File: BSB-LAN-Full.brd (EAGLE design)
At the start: 86.5 x 33 mm, 121 parts, among them IC1 LAN8710A-EZC, IC2 TPS2375D, IC3 TX4138, IC4 SY8089AAAC, IC6 CH340X, Q1 BC847, Q2 BC857, Q3 BC847, Q4 WPM2015-3/TR, Q5 BC847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

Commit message: Rename Connector Footprint
Remove special characters
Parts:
- BSB: device BSB-LAN:MKDSN1,5/2-5,08 -> BSB-LAN:MKDSN1_5-2-5_08
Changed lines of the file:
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@@
 <attribute name="NAME" x="27.2" y="32.4" size="0.8" layer="26" font="vector" ratio="15" rot="MR0" align="center"/>
 </element>
-<element name="BSB" library="BSB-LAN" package="MKDSN1,5/2-5,08" value="MKDSN1,5/2-5,08" x="4.96" y="26.66" smashed="yes" rot="R270">
+<element name="BSB" library="BSB-LAN" package="MKDSN1_5-2-5_08" value="MKDSN1,5/2-5,08" x="4.96" y="26.66" smashed="yes" rot="R270">
 <attribute name="NAME" x="11.15" y="31.47" size="1.2" layer="25" font="vector" ratio="15" align="center"/>
 <attribute name="OC_NEWARK" value="30M2397" x="4.96" y="26.66" size="1.778" layer="27" rot="R270" display="off"/>

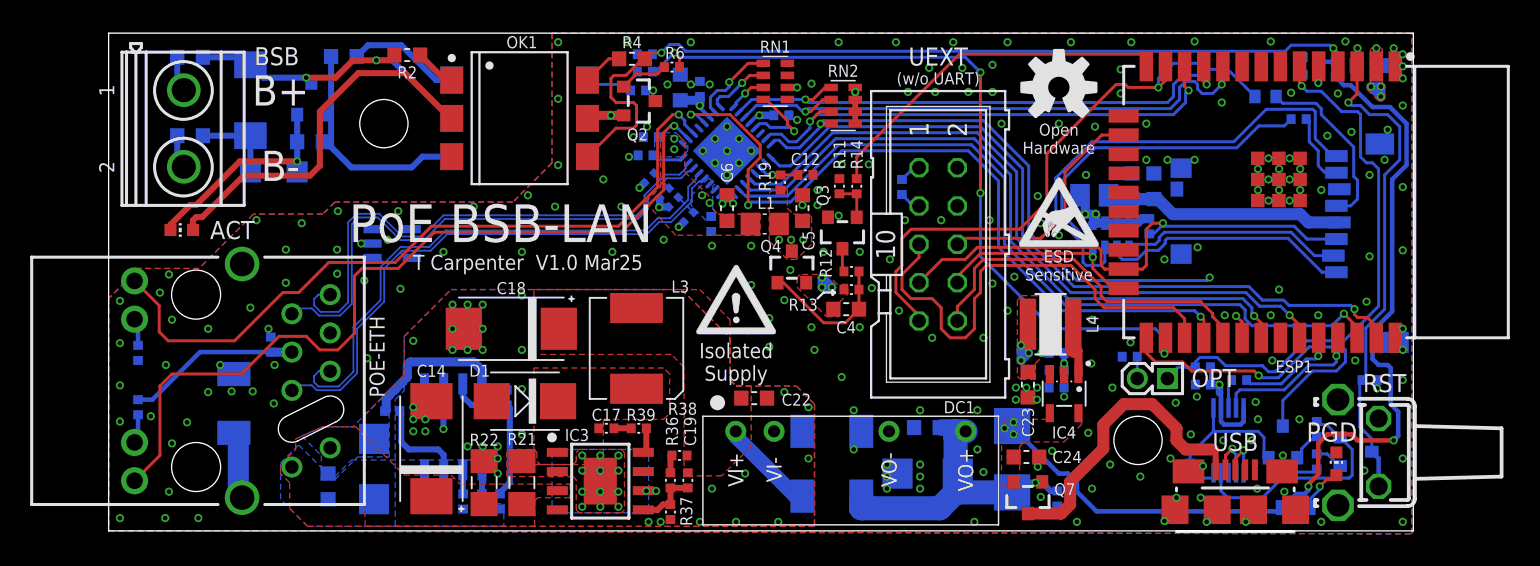
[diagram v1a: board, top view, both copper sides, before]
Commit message: Fix USB Position and Pinout UEXT 3/4
1. Move the microUSB port inward so that it doesn't foul the enclosure.
2. Pinout UEXT 3/4 to the spare GPIO pins 32/33. The correct two pins are in use by the BSB interface so they were previously left unconnected on UEXT, but we might as well have other GPIOs connected so we have a fully populated expansion header.
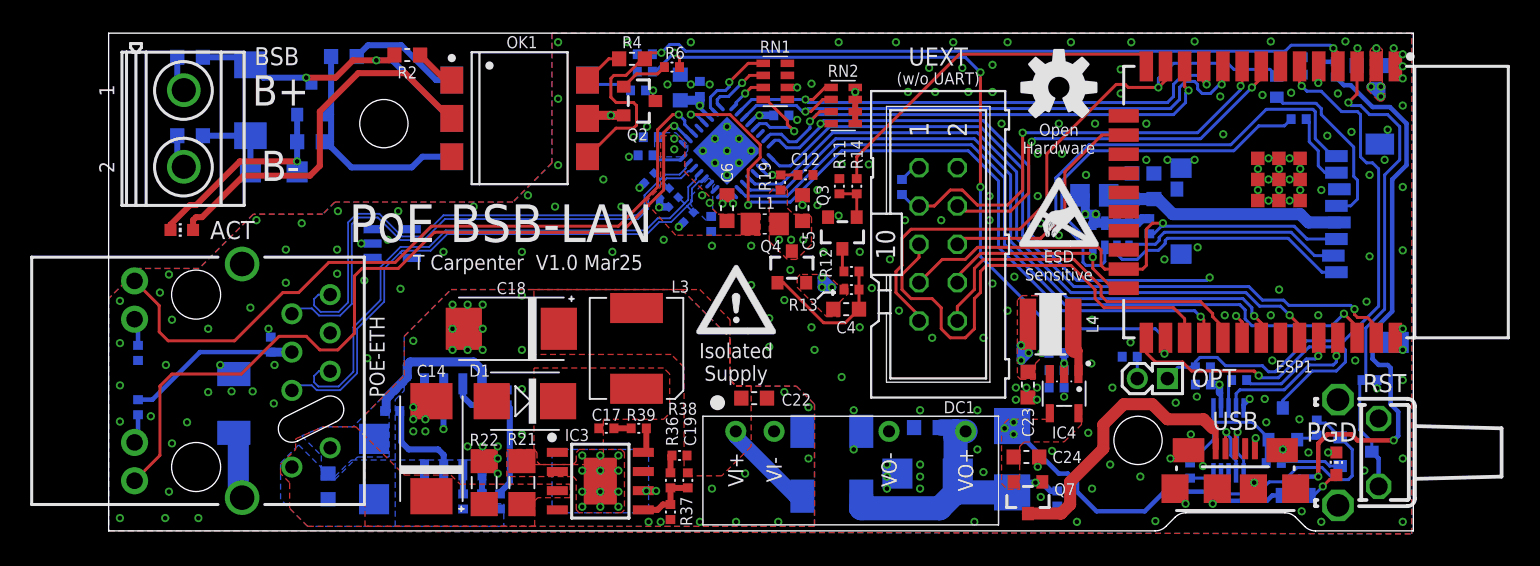
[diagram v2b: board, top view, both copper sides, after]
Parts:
- moved R46 2.85 mm to (77.2, 4.50), turned to 0 degrees
- moved USB 1.40 mm to (74.7, 2.80)
- moved Q5 1.20 mm to (77.8, 7.05)
- moved R33 0.99 mm to (77.5, 29.4), turned to 270 degrees
- moved R48 0.80 mm to (78.7, 2.35)
- moved R45 0.10 mm to (80.1, 6.85)
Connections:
- new net UEXT-RX: ESP1.8, UEXT.4
- net UEXT-TX: now also ESP1.9
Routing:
- net UEXT-TX: track 1.44 -> 30.6 mm, vias 0 -> 2
- net UEXT-RX: track 0.00 -> 26.6 mm, vias 0 -> 2
- net CH340-!DTR: track 13.3 -> 10.1 mm
- net +3.3V: track 53.3 -> 50.6 mm, vias 16 -> 17
- net N$4: track 1.88 -> 4.12 mm
- net USB-D+: track 3.03 -> 4.68 mm
- net USB-D-: track 3.29 -> 4.54 mm
- net ESP-GPIO0: track 23.6 -> 22.4 mm
- net USB-VBUS: track 20.3 -> 19.3 mm
- net ESP-SD-CLK: track 39.4 -> 40.3 mm
- net N$2: track 2.45 -> 1.60 mm
- net PWR-LED: track 3.30 -> 2.58 mm
- net GND: vias 223 -> 227
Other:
- outline, holes or cut-outs redrawn

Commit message: Assign JLC Part Numbers
Minor adaptions to available passive parts and packages and now all parts are available in JLCs inventory. LCSC_PART attributes have been applied to aid in BoM creation.

Additionally add extra ESD protection for USB port.
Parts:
- added U2: ESDS314DBV, BSB-LAN:DBV0005A-SOT23
- C14: value 15uF 100V -> 22uF 100V; device BSB-LAN:SMC_D -> BSB-LAN:PANASONIC_D
- C22, C24, C25: device BSB-LAN:C0603 -> BSB-LAN:C0805
- R39: value 4.7R -> 10R; device BSB-LAN:R0402 -> BSB-LAN:R0603L
- U$3: value OSHW-LOGOM -> DNI
- moved C14 1.12 mm to (20.9, 4.45), turned to 270 degrees
- moved L3 0.65 mm to (35.6, 12.3)
- moved R23 0.64 mm to (26.4, 1.50), turned to 0 degrees
- moved U$1 0.63 mm to (42.2, 15.0)
- moved D1 0.61 mm to (28.2, 8.70)
- moved R22 0.55 mm to (25.4, 3.20)
- moved R21 0.45 mm to (27.9, 3.20)
- moved C24 0.32 mm to (61.0, 5.15)
- moved R39 0.27 mm to (35.4, 6.90)
- moved C25 0.25 mm to (54.4, 7.05)
- moved IC3 0.20 mm to (32.8, 3.30)
- moved C17 0.14 mm to (33.1, 6.90)
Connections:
- net ESP-BUTTON: now also U2.3
- net ESP-EN: now also U2.1
- net GND: now also U2.2
- net USB-D+: now also U2.5
- net USB-D-: now also U2.4
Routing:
- net ESP-EN: track 34.6 -> 42.7 mm, vias 2 -> 3
- net ESP-BUTTON: track 36.5 -> 40.8 mm
- net USB-D+: track 4.68 -> 6.39 mm
- net POE-UVLO: track 10.2 -> 11.2 mm
- net USB-D-: track 4.54 -> 5.48 mm
- net POE-PG: track 23.8 -> 23.4 mm, vias 3 -> 2
- net GND: vias 227 -> 229

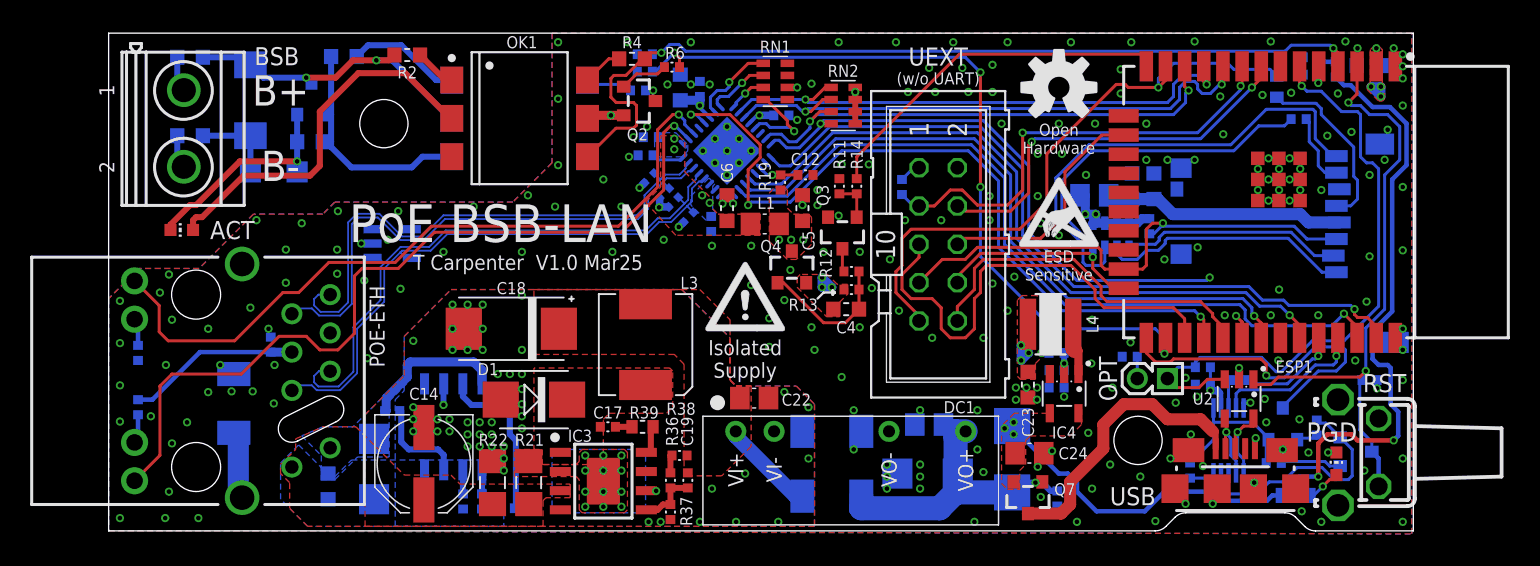
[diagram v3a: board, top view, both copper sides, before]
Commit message: Begin optimising for assembly cost
Trying to reduce the number of different components, as well as instances where the same component is used on two sides of the board (incurs double assembly setup fee).
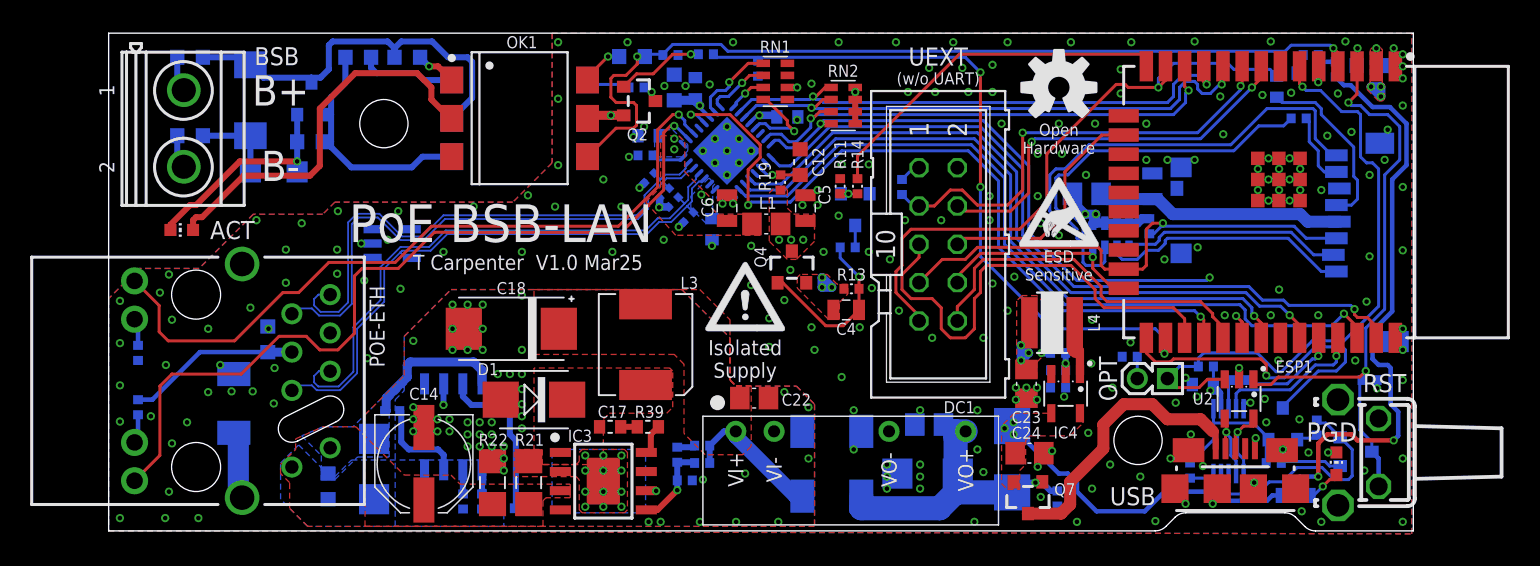
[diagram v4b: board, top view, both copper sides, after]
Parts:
- C10, C11, C17, C26, C27, C8, C9: device BSB-LAN:C0402 -> BSB-LAN:C0603L
- C12, C3: device BSB-LAN:C0402 -> BSB-LAN:C0603
- C15, C16, C4, C5, C6: device BSB-LAN:C0603 -> BSB-LAN:C0805L
- C23: device BSB-LAN:C0603 -> BSB-LAN:C0805
- moved R8 7.50 mm to (43.0, 30.6), turned to 90 degrees
- moved R6 2.41 mm to (39.6, 31.6), flipped to the bottom, turned to 180 degrees
- moved R37 2.30 mm to (38.2, 3.35), flipped to the bottom, turned to 180 degrees
- moved Q3 1.77 mm to (49.5, 21.4), flipped to the bottom
- moved R36 1.76 mm to (37.7, 5.05), flipped to the bottom
- moved R5 1.70 mm to (37.2, 31.6), turned to 180 degrees
- moved R38 1.63 mm to (39.4, 5.65), flipped to the bottom, turned to 0 degrees
- moved R12 1.62 mm to (49.0, 18.8), flipped to the bottom
- moved C19 1.49 mm to (39.4, 4.50), flipped to the bottom, turned to 0 degrees
- moved R1 0.95 mm to (16.6, 31.4)
- moved C12 0.92 mm to (45.9, 24.4), turned to 90 degrees
- moved L2 0.51 mm to (64.8, 22.4)
- moved C11 0.41 mm to (45.0, 27.4)
- moved C3 0.40 mm to (10.6, 12.7)
- moved C7 0.40 mm to (37.5, 29.4)
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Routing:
- net BSB+: track 21.3 -> 26.8 mm, vias 2 -> 0
- net BSB-TXD: track 52.7 -> 47.3 mm, vias 4 -> 3
- net POE-5V0: track 6.39 -> 9.67 mm
- net TXD-B: track 3.24 -> 5.84 mm, vias 0 -> 1
- net ETH-PWR-G: track 9.37 -> 11.7 mm, vias 0 -> 1
- net POE-DC-FB: track 4.00 -> 5.64 mm, vias 0 -> 1
- net BSB-TX-B: track 7.57 -> 6.39 mm
- net SD-DAT1: track 31.8 -> 32.8 mm
- net ESP-SD-DATA: track 36.3 -> 37.3 mm
- net ETH-PWR-B: track 2.70 -> 1.70 mm, vias 0 -> 1
- net EMAC-RXD0: track 37.5 -> 36.8 mm
- net BSB-RX-K: track 25.2 -> 25.8 mm
- net RXD-B: track 2.68 -> 2.87 mm, vias 0 -> 1
- net BSB-RX-A: track 2.79 -> 2.73 mm, vias 0 -> 1

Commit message: Move LAN IC to Top Side
With LAN IC on the top side, the board could be manufactered with only the top-side components populated, and with the exception of the uSD card all the bottom side parts are then relatively easy to hand solder with care.
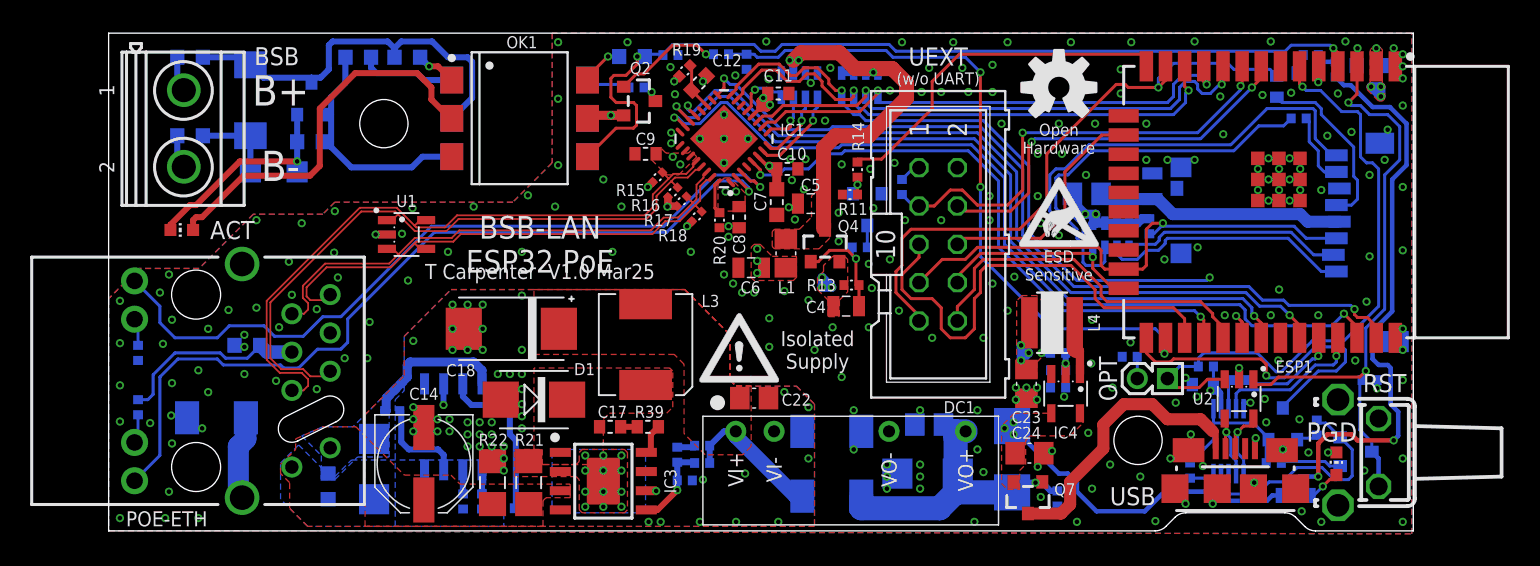
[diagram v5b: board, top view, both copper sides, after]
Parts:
- C12: device BSB-LAN:C0603 -> BSB-LAN:C0603L
- moved C7 10.2 mm to (44.3, 21.8), flipped to the top, turned to 270 degrees
- moved R19 9.75 mm to (38.2, 30.5), turned to 225 degrees
- moved C12 8.51 mm to (39.1, 29.7), turned to 45 degrees
- moved C10 8.11 mm to (45.0, 24.0), flipped to the top, turned to 0 degrees
- moved C8 8.07 mm to (41.8, 20.8), flipped to the top, turned to 270 degrees
- moved C9 6.66 mm to (35.6, 25.0), flipped to the top, turned to 180 degrees
- moved R20 6.52 mm to (40.5, 20.6), flipped to the top, turned to 90 degrees
- moved C6 4.26 mm to (42.6, 17.4), turned to 180 degrees
- moved R18 4.05 mm to (39.0, 20.9), flipped to the top, turned to 45 degrees
- moved U$1 3.42 mm to (41.8, 11.6)
- moved R15 3.35 mm to (36.4, 23.4), flipped to the top, turned to 225 degrees
- moved Q4 2.61 mm to (47.5, 18.9)
- moved L1 2.34 mm to (44.9, 18.4), turned to 270 degrees
- moved RN2 1.74 mm to (49.8, 29.6), flipped to the bottom, turned to 0 degrees
- moved C11 1.66 mm to (44.4, 29.0), flipped to the top, turned to 0 degrees
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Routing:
- net ETH-VDDIO: track 5.15 -> 44.3 mm
- net EMAC-CLKOUT: track 51.0 -> 39.6 mm, vias 3 -> 2
- net EMAC-TXD0: track 44.7 -> 51.4 mm, vias 1 -> 2
- net ETH-TD_N: track 38.4 -> 44.3 mm
- net EMAC-TXD1: track 51.9 -> 57.6 mm, vias 1 -> 2
- net EMAC-TXEN: track 46.7 -> 52.4 mm, vias 1 -> 2
- net ETH-TD_P: track 38.2 -> 43.7 mm
- net EMAC-MDC: track 50.5 -> 55.0 mm, vias 1 -> 2
- net EMAC-MDIO: track 42.9 -> 47.3 mm
- net GND: track 4.00 -> 0.00 mm, vias 229 -> 239
- net ETH-PWR-G: track 11.7 -> 7.74 mm
- net EMAC-RX-CRSDV: track 33.7 -> 36.8 mm
- net ETH-RD_P: track 37.1 -> 34.4 mm
- net +3.3V: track 50.9 -> 53.3 mm
- net ETH-RD_N: track 37.3 -> 35.0 mm
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- added copper zone on layer 15, net ETH-VDDA
- removed copper zone on layer 16, net ETH-VDDA
- removed copper zone on layer 2, net ETH-VDDIO
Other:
- board text added: "BSB-LAN ESP32 PoE"
- board text removed: "PoE BSB-LAN"

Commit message: Correct CNMB Footprint Keepout
The zone was measured wrong from the model. Need the backside components to be further from the edge. Fix the board layout to achieve this.
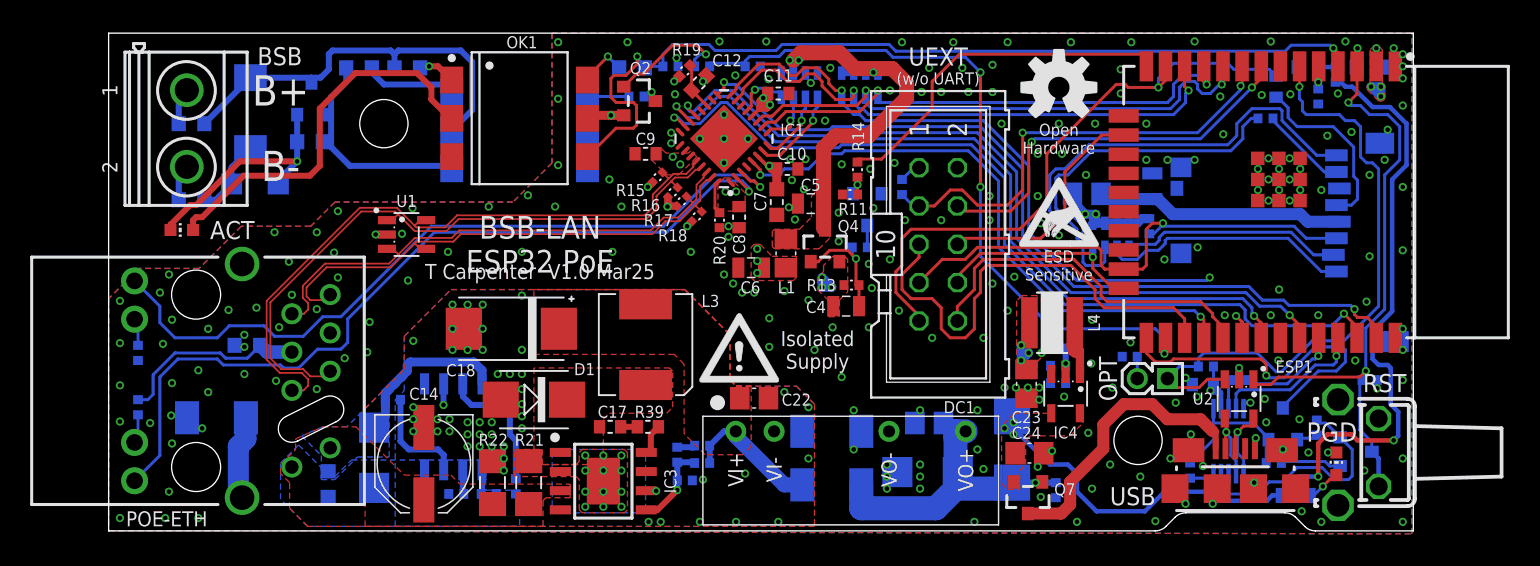
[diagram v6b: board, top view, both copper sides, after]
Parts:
- moved R10 4.40 mm to (5.50, 27.0)
- moved R9 4.25 mm to (5.50, 21.9)
- moved R44 2.80 mm to (80.2, 28.8), turned to 270 degrees
- moved R31 2.20 mm to (76.7, 27.4)
- moved R23 1.57 mm to (27.0, 2.95), turned to 270 degrees
- moved D2 1.48 mm to (9.70, 23.0)
- moved R6 1.48 mm to (39.4, 30.8)
- moved D3 0.85 mm to (9.40, 27.7)
- moved OK2 0.80 mm to (27.2, 26.6)
- moved R25 0.75 mm to (18.9, 8.70)
- moved C20 0.75 mm to (48.0, 3.05)
- moved D4 0.75 mm to (17.6, 4.85)
- moved R4 0.75 mm to (34.7, 30.7)
- moved R5 0.75 mm to (37.2, 30.8)
- moved R1 0.70 mm to (16.6, 30.7)
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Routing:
- net POE-UVLO: track 11.2 -> 9.13 mm
- net BSB-TXD: track 46.3 -> 48.2 mm
- net ESP-SD-DATA: track 37.3 -> 35.6 mm
- net BSB-: track 14.3 -> 15.6 mm
- net BSB-RXD: track 59.9 -> 61.0 mm
- net SD-DAT0: track 4.85 -> 5.76 mm
- net +5.0V: track 61.6 -> 62.4 mm
- net TXD-B: track 7.34 -> 8.18 mm
- net BSB-TX-E: track 16.1 -> 15.3 mm
- net POE-DET: track 6.31 -> 6.98 mm
- net +3.3V: track 53.3 -> 52.8 mm

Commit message: Correct PoE IC Part Number
The LCSC_PART selected was the TPS2376DDA but the schematic value was TPS2375D, This actually has a slightly different footprint - the DDA has a thermal pad.

Update to account for the change.
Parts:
- IC2: value TPS2375D -> TPS2376D
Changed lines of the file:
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@@
 <layer number="220" name="220bmp" color="21" fill="1" visible="no" active="no"/>
 <layer number="221" name="221bmp" color="22" fill="1" visible="no" active="no"/>
-<layer number="222" name="222bmp" color="7" fill="1" visible="no" active="yes"/>
+<layer number="222" name="222bmp" color="7" fill="1" visible="yes" active="yes"/>
 <layer number="223" name="223bmp" color="24" fill="1" visible="no" active="no"/>
 <layer number="224" name="224bmp" color="25" fill="1" visible="no" active="no"/>
@@
 <attribute name="LCSC_PART" value="C113803" x="14.55" y="3.1" size="1.778" layer="28" rot="MR270" display="off"/>
 </element>
-<element name="IC2" library="BSB-LAN" package="SOIC8" value="TPS2375D" x="22.85" y="6.9" smashed="yes" rot="MR0">
-<attribute name="LCSC_PART" value="C544899" x="22.85" y="6.9" size="1" layer="28" font="vector" ratio="15" rot="MR0" display="off"/>
+<element name="IC2" library="BSB-LAN" package="SOIC8" value="TPS2376D" x="22.85" y="6.9" smashed="yes" rot="MR0">
+<attribute name="LCSC_PART" value="C2859892" x="22.85" y="6.9" size="1" layer="28" font="vector" ratio="15" rot="MR0" display="off"/>
 <attribute name="NAME" x="21.2" y="11.1575" size="0.8" layer="26" font="vector" ratio="15" rot="MR180" align="center"/>
 </element>
